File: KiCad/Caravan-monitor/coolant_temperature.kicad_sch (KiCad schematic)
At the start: 3 parts, among them J4 Coolant temp

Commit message: Schematics done
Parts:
- C21: footprint Capacitor_SMD:C_0805_2012Metric_Pad1.18x1.45mm_HandSolder -> Capacitor_SMD:C_0402_1005Metric_Pad0.74x0.62mm_HandSolder
- R16: footprint Resistor_SMD:R_0805_2012Metric_Pad1.20x1.40mm_HandSolder -> Resistor_SMD:R_0402_1005Metric_Pad0.72x0.64mm_HandSolder
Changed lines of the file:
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@@
 			)
 		)
-		(property "Footprint" "Capacitor_SMD:C_0805_2012Metric_Pad1.18x1.45mm_HandSolder"
+		(property "Footprint" "Capacitor_SMD:C_0402_1005Metric_Pad0.74x0.62mm_HandSolder"
 			(at 163.5252 99.06 0)
 			(effects
@@
 			)
 		)
-		(property "Footprint" "Resistor_SMD:R_0805_2012Metric_Pad1.20x1.40mm_HandSolder"
+		(property "Footprint" "Resistor_SMD:R_0402_1005Metric_Pad0.72x0.64mm_HandSolder"
 			(at 140.462 85.09 90)
 			(effects

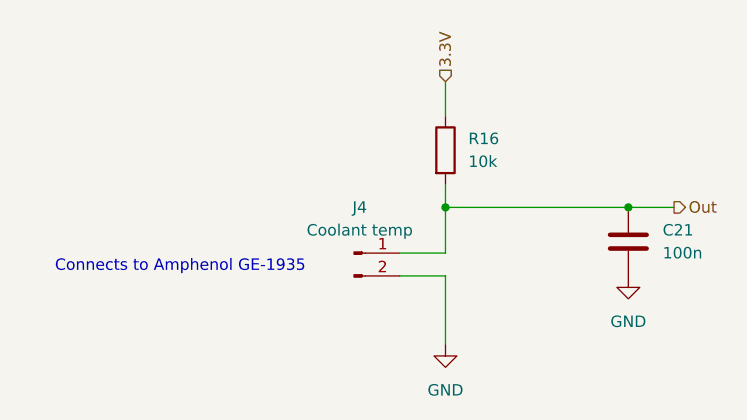
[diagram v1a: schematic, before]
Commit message: Schematic updates
Parts changed for JLCPCB assembly compatibility
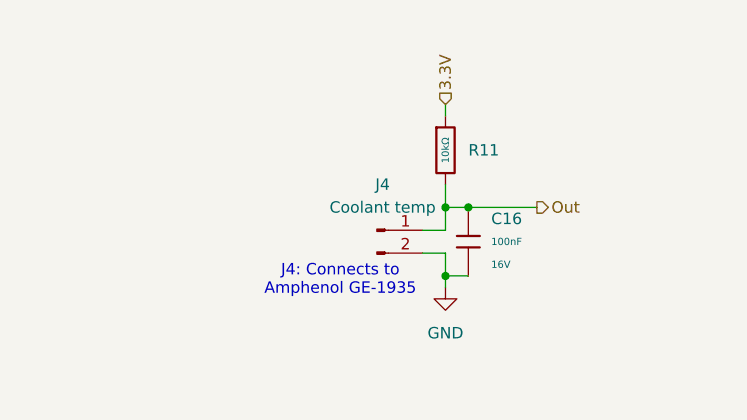
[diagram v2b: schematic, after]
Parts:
- removed C21: 100n, Capacitor_SMD:C_0402_1005Metric_Pad0.74x0.62mm_HandSolder, symbol Device:C
- removed R16: 10k, Resistor_SMD:R_0402_1005Metric_Pad0.72x0.64mm_HandSolder, symbol Device:R
- added C16: 100nF, PCM_JLCPCB:C_0402, symbol PCM_JLCPCB-Capacitors:0402,100nF
- added R11: 10kΩ, PCM_JLCPCB:R_0402, symbol PCM_JLCPCB-Resistors:0402,10kΩ
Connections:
- net 3.3V: now also R11.1
- net GND: now also C16.2
- net Out: now also C16.1, R11.2
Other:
- note added: "J4: Connects to Amphenol GE-1935"
- note removed: "Connects to Amphenol GE-1935"
- moved on the sheet: J4
